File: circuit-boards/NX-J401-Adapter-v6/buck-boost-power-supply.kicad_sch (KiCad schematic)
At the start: 58 parts, among them Q2 CSD19534Q5A, Q3 CSD19534Q5A, Q4 CSD17578Q5A, Q5 CSD17578Q5A

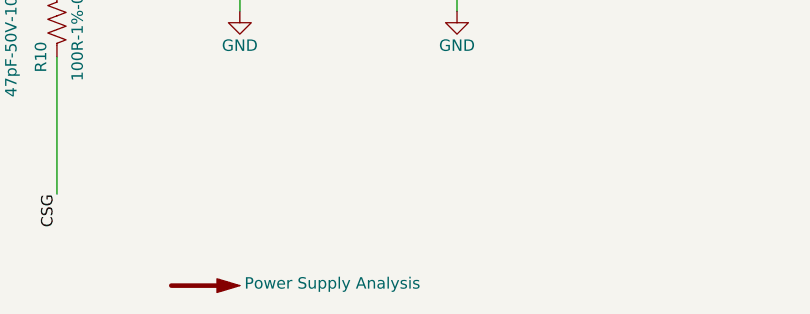
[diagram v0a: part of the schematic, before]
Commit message: Changed canable to use 3.3V power form USB to use key-e connector that breaks out USB and 3V3
Signed-off-by: Scott Berman <sgberman1@gmail.com>
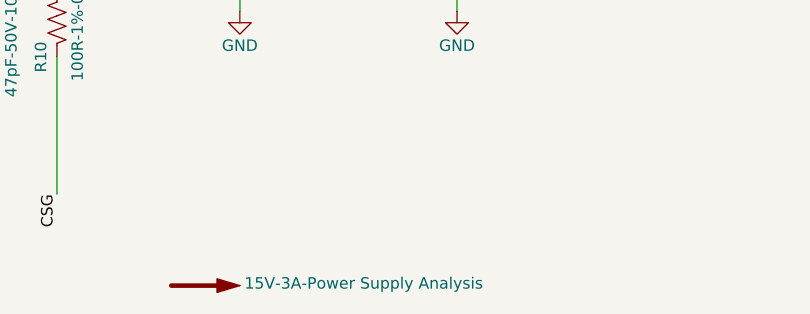
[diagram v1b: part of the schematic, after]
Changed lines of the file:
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@@
 			)
 		)
-		(property "Value" "Power Supply Analysis"
+		(property "Value" "15V-3A-Power Supply Analysis"
 			(at 142.748 241.046 0)
 			(show_name no)

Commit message: Added ideal diode circuit for reverse polarity and output or-ing
Signed-off-by: Scott Berman <sgberman1@gmail.com>
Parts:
- removed C33, C34, C6: 10uF-50V-10%-X7R-1210, Capacitor_SMD:C_1210_3225Metric, symbol Device:C_US

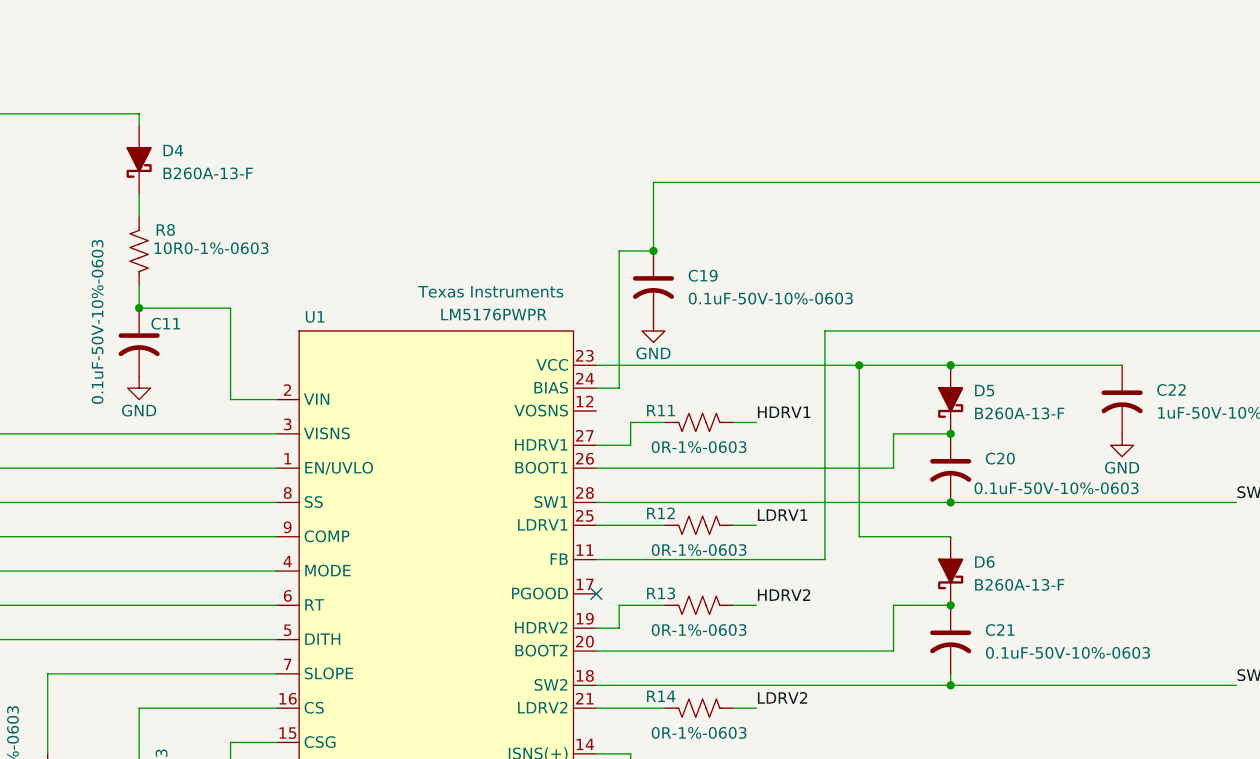
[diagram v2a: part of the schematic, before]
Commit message: Initial fully routed PCB
Signed-off-by: Scott Berman <sgberman1@gmail.com>
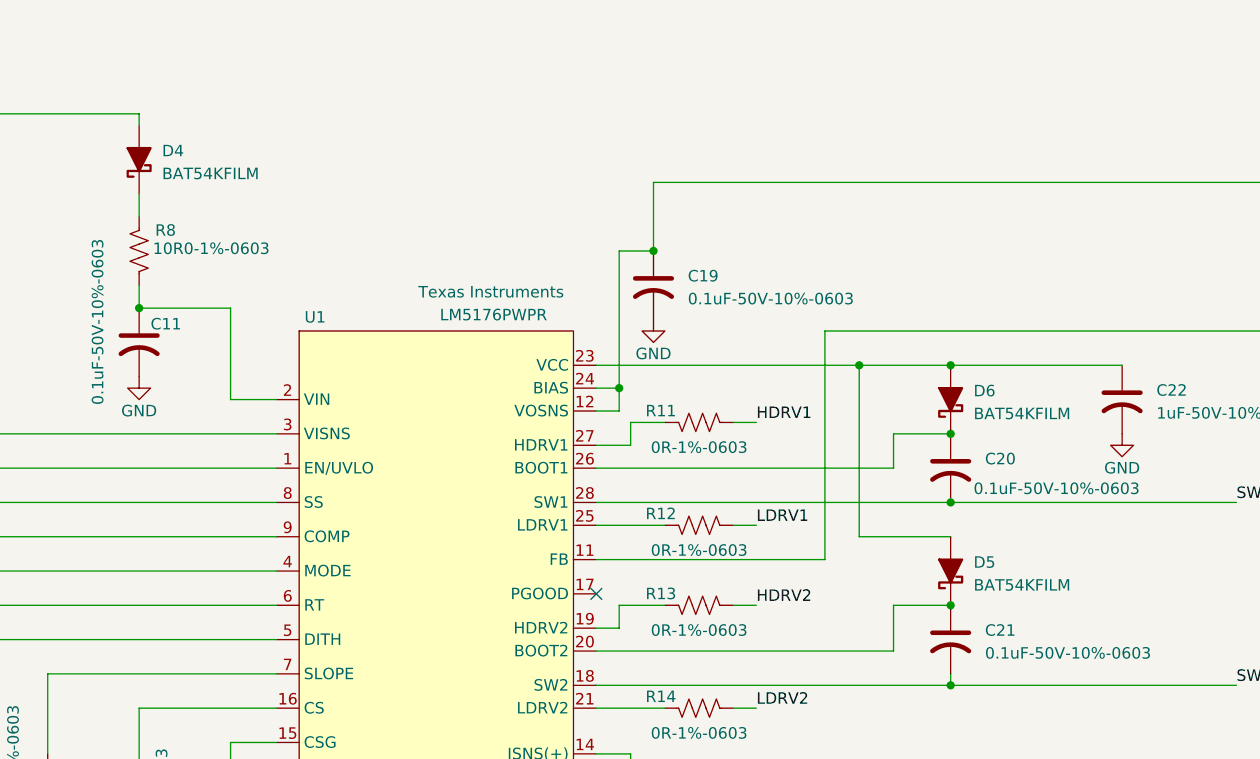
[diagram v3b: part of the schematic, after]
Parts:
- D4, D5, D6: value B260A-13-F -> BAT54KFILM; footprint Diode_SMD:D_SMA -> Diode_SMD:D_SOD-523; JLCPCB P/N C109094 -> C283259; MFG Diodes Inc -> STmicro; MFG P/N B260A-13-F -> STMicroelectronics
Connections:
- net +V_OUT: now also U1.12 (VOSNS)
- net at C21.1, U1.20 (BOOT2): now also D5.1 (K); no longer D6.1 (K)
- net at C20.1, U1.26 (BOOT1): now also D6.1 (K); no longer D5.1 (K)

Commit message: Initial complete routing
Signed-off-by: Scott Berman <sgberman1@gmail.com>
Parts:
- C12: renamed from C14; KiLib_Generator (none) -> SMD_2terminal_chip_molded
- C13: renamed from C12; KiLib_Generator (none) -> SMD_2terminal_chip_molded
- C14: renamed from C16; KiLib_Generator (none) -> SMD_2terminal_chip_molded
- C15, C27: KiLib_Generator (none) -> SMD_2terminal_chip_molded
- C16: renamed from C28; KiLib_Generator (none) -> SMD_2terminal_chip_molded
- C17: renamed from C25; KiLib_Generator (none) -> SMD_2terminal_chip_molded
- C18: renamed from C26; KiLib_Generator (none) -> SMD_2terminal_chip_molded
- C19: renamed from C32; KiLib_Generator (none) -> SMD_2terminal_chip_molded
- C20: renamed from C31; KiLib_Generator (none) -> SMD_2terminal_chip_molded
- C23: renamed from C8; KiLib_Generator (none) -> SMD_2terminal_chip_molded
- C24: renamed from C18; KiLib_Generator (none) -> SMD_2terminal_chip_molded
- C25: renamed from C17; KiLib_Generator (none) -> SMD_2terminal_chip_molded
- C26: renamed from C7; KiLib_Generator (none) -> SMD_2terminal_chip_molded
- C28: renamed from C24; KiLib_Generator (none) -> SMD_2terminal_chip_molded
- C29: renamed from C23; KiLib_Generator (none) -> SMD_2terminal_chip_molded
- C30: renamed from C29; KiLib_Generator (none) -> SMD_2terminal_chip_molded
- C31: renamed from C30; KiLib_Generator (none) -> SMD_2terminal_chip_molded
- C32: renamed from C20; KiLib_Generator (none) -> SMD_2terminal_chip_molded
- C33: renamed from C19; KiLib_Generator (none) -> SMD_2terminal_chip_molded
- C34: renamed from C22; KiLib_Generator (none) -> SMD_2terminal_chip_molded
- C35: renamed from C21; KiLib_Generator (none) -> SMD_2terminal_chip_molded
- C37: renamed from C13; KiLib_Generator (none) -> SMD_2terminal_chip_molded
- C43: renamed from C10; KiLib_Generator (none) -> SMD_2terminal_chip_molded
- C47: renamed from C11; KiLib_Generator (none) -> SMD_2terminal_chip_molded
- C48: renamed from C9; KiLib_Generator (none) -> SMD_2terminal_chip_molded
- C49: renamed from C2; KiLib_Generator (none) -> SMD_2terminal_chip_molded
- C50: renamed from C5; KiLib_Generator (none) -> SMD_2terminal_chip_molded
- C51: renamed from C4; KiLib_Generator (none) -> SMD_2terminal_chip_molded
- C52: renamed from C3; KiLib_Generator (none) -> SMD_2terminal_chip_molded
- R10: renamed from R14; KiLib_Generator (none) -> SMD_2terminal_chip_molded
- R11: renamed from R13; KiLib_Generator (none) -> SMD_2terminal_chip_molded
- R12: renamed from R9; KiLib_Generator (none) -> SMD_2terminal_chip_molded
- R13: renamed from R10; KiLib_Generator (none) -> SMD_2terminal_chip_molded
- R14: renamed from R3; KiLib_Generator (none) -> SMD_2terminal_chip_molded
- R15: renamed from R4; KiLib_Generator (none) -> SMD_2terminal_chip_molded
- R17: renamed from R8; KiLib_Generator (none) -> SMD_2terminal_chip_molded
- R18: renamed from R6; KiLib_Generator (none) -> SMD_2terminal_chip_molded
- R19: renamed from R5; KiLib_Generator (none) -> SMD_2terminal_chip_molded
- R20: renamed from R7; KiLib_Generator (none) -> SMD_2terminal_chip_molded
- R21: renamed from R2; KiLib_Generator (none) -> SMD_2terminal_chip_molded
- R22: renamed from R17; KiLib_Generator (none) -> SMD_2terminal_chip_molded
- R23: renamed from R16; KiLib_Generator (none) -> SMD_2terminal_chip_molded
- R6: renamed from R15; KiLib_Generator (none) -> SMD_2terminal_chip_molded
- R8: renamed from R11; KiLib_Generator (none) -> SMD_2terminal_chip_molded
- R9: renamed from R12; KiLib_Generator (none) -> SMD_2terminal_chip_molded
- renumbered D6 to D1, D5 to D2, L1 to L2, Q5 to Q4, Q2 to Q6, Q4 to Q7, U1 to U5
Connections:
- net Vcc: now reaches C34.1, D1.2 (A), D2.2 (A), U5.23 (VCC)

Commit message: minor fixes
Signed-off-by: Scott Berman <sgberman1@gmail.com>
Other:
- company: (none) -> SPACE COOKIES FRC TEAM 1868
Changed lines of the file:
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@@
 	(title_block
 		(title "NX J401 Adapter")
-		(date "2026-05-10")
+		(date "2026-05-25")
 		(rev "6")
+		(company "SPACE COOKIES FRC TEAM 1868")
 	)
 	(junction

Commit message: Updates
Signed-off-by: Scott Berman <sgberman1@gmail.com>
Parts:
- C12, C13, C14, C15, C16, C17, C18, C19, C20, C23, C24, C25, C26, C27, C28, C29, C30, C31, C43: footprint Capacitor_SMD:C_1210_3225Metric -> NX-J401-Adapter:C_1210_3225Metric; symbol Device:C_US -> NX-J401-Adapter:C_US
- C32, C33, C34, C35, C37, C47, C48, C49, C50, C51, C52: footprint Capacitor_SMD:C_0603_1608Metric -> NX-J401-Adapter:C_0603_1608Metric; symbol Device:C_US -> NX-J401-Adapter:C_US
- D1, D2, D4: footprint Diode_SMD:D_SOD-523 -> NX-J401-Adapter:D_SOD-523
- L2: symbol Device:L_Iron -> NX-J401-Adapter:L_Iron
- Q3, Q4, Q6, Q7: symbol Transistor_FET:CSD19534Q5A -> NX-J401-Adapter:CSD19534Q5A
- R10, R11, R12, R13, R14, R15, R17, R18, R19, R20, R21, R22, R23, R8, R9: footprint Resistor_SMD:R_0603_1608Metric -> NX-J401-Adapter:R_0603_1608Metric; symbol Device:R_US -> NX-J401-Adapter:R_US
- R6: footprint Resistor_SMD:R_2512_6332Metric -> NX-J401-Adapter:R_2512_6332Metric; symbol Device:R_US -> NX-J401-Adapter:R_US
